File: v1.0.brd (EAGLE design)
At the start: 160 x 100 mm, 142 parts, among them J1 DC-044-A, J2 MICROSD-9P, J3 2p-2.54, J4 2p-2.54, Q1 SI4532ADY, Q3 6pF@32.7680kHz, U1 MCP23017-E/SO, U10 74HC139N, U11 BZX84C30, U2 MCP79412-I/SN, U3 LOPY, U4 GROVE_DC&DC, U5 LM1085IT-5.0, U6 FT232RL-SSOP28, U7 2x14p-2.54, U8 FT232RL-SSOP28, U9 SP483ECN-L, X1 JST-XH-05-PIN-ROUND-PAD, X10 JST-XH-07-PIN-ROUND-PAD, X11 JST-XH-07-PIN-ROUND-PAD, X12 JST-XH-07-PIN-ROUND-PAD, X13 JST-XH-05-PIN-ROUND-PAD, X14 JST-XH-05-PIN-ROUND-PAD, X15 JST-XH-05-PIN-ROUND-PAD, X16 JST-XH-05-PIN-ROUND-PAD, X17 JST-XH-05-PIN-ROUND-PAD, X18 JST-XH-05-PIN-ROUND-PAD, X19 JST-XH-05-PIN-ROUND-PAD, X2 JST-XH-05-PIN-ROUND-PAD, X20 JST-XH-05-PIN-ROUND-PAD, X21 JST-XH-05-PIN-ROUND-PAD, X23 JST-XH-05-PIN-ROUND-PAD, X24 JST-XH-07-PIN-ROUND-PAD, X25 JST-XH-07-PIN-ROUND-PAD, X26 JST-XH-07-PIN-ROUND-PAD, X27 JST-XH-07-PIN-ROUND-PAD, X28 JST-XH-05-PIN-ROUND-PAD, X3 JST-XH-05-PIN-ROUND-PAD, X4 JST-XH-07-PIN-ROUND-PAD, X5 JST-XH-07-PIN-ROUND-PAD, X6 JST-XH-07-PIN-ROUND-PAD, X7 JST-XH-07-PIN-ROUND-PAD, X8 JST-XH-07-PIN-ROUND-PAD, X9 JST-XH-07-PIN-ROUND-PAD

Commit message: polyfuses
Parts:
- removed X26: JST-XH-07-PIN-ROUND-PAD, Rembrandt Electronics - JST XH Connectors v1-0 2:JST-XH-07-PACKAGE-ROUND-PAD
- added F23, F24, F25, F26, F27, F28, F29, F30, F31, F32, F33, F34, F35, F36, F37, F38, F39, F40, F41, F42, F43, F44, F45, F46, F47: SMD1206R500SF, Seeed-Fuse:F1206
- added X22: JST-XH-07-PIN-ROUND-PAD, Rembrandt Electronics - JST XH Connectors v1-0 2:JST-XH-07-PACKAGE-ROUND-PAD
- moved X12 1177.6 mm to (-1008.4, -552.5)
- moved X10 1103.3 mm to (-1008.4, -529.6)
- moved X25 984.9 mm to (-1033.8, -621.0)
- moved X24 981.9 mm to (-1033.8, -598.2)
- moved F2 268.6 mm to (-1022.4, -518.2)
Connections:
- new net +5V1: F24.1, F24.2, X10.1
- new net +5V2: F30.1, F30.2, X12.1
- new net +5V3: F40.1, F40.2, X22.1
- new net +5V4: F42.1, F42.2, X24.1
- new net +5V5: F44.1, F44.2, X25.1
- new net 3V3_SMOOTH1: F27.1, F27.2, X10.2
- new net 3V3_SMOOTH2: F31.1, F31.2, X12.2
- new net 3V3_SMOOTH3: F41.1, F41.2, X22.2
- new net 3V3_SMOOTH4: F43.1, F43.2, X24.2
- new net 3V3_SMOOTH5: F45.1, F45.2, X25.2
- new net N$57: F25.2, X6.2
- new net N$58: F23.2, X6.1
- new net N$59: F3.2, X5.1
- new net N$60: F26.2, X8.1
- new net N$61: F35.2, X23.2
- new net N$62: F47.2, X28.2
- net +5V: now also F23.1, F26.1, F28.1, F28.2, F32.1, F32.2, F34.1, F34.2, F36.1, F36.2, F38.1, F38.2, F46.1, F46.2; no longer X10.1, X12.1, X24.1, X25.1, X26.1, X6.1, X8.1
- net 3V3_SMOOTH: now also F2.1, F2.2, F25.1, F29.1, F29.2, F33.1, F33.2, F35.1, F37.1, F37.2, F39.1, F39.2, F47.1; no longer X10.2, X12.2, X23.2, X24.2, X25.2, X26.2, X28.2, X6.2
- net ADC3+: now also X22.4; no longer X24.4
- net ADC3-: now also X22.5; no longer X24.5
- net ADC4+: now also X22.6; no longer X24.6
- net ADC4-: now also X22.7; no longer X24.7
- net ADC5+: now also X24.4; no longer X25.4
- net ADC5-: now also X24.5; no longer X25.5
- net ADC6+: now also X24.6; no longer X25.6
- net ADC6-: now also X24.7; no longer X25.7
- net ADC7+: now also X25.4; no longer X26.4
- net ADC7-: now also X25.5; no longer X26.5
- net ADC8+: now also X25.6; no longer X26.6
- net ADC8-: now also X25.7; no longer X26.7
- net GND: now also X22.3; no longer X26.3
- net SPI_MISO: now also X10.5, X12.5; no longer X10.4, X12.4
- net SPI_MOSI: now also X10.4, X12.4; no longer X10.5, X12.5

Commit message: I think I am done?
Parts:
- added SW1, SW2: SW-200D, Seeed-Switch:SW2-12.7-12.0X3.6X3.6MM
- R10, R9: value 1K -> 100R; device Seeed-Resistor-2016:R0603 -> Seeed-Resistor:PR-D2.3XL6.5MM
- R6: value 1K -> 220R; device Seeed-Resistor-2016:R0603 -> Seeed-Resistor:PR-D2.3XL6.5MM
- R7: value 1K -> 330K; device Seeed-Resistor-2016:R0603 -> Seeed-Resistor:PR-D2.3XL6.5MM
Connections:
- new net N$65: Q1.1, R17.1, SW2.1
- net GND: now also SW1.2, SW2.2; no longer Q1.1, R17.1
- net N$23: now also SW1.1

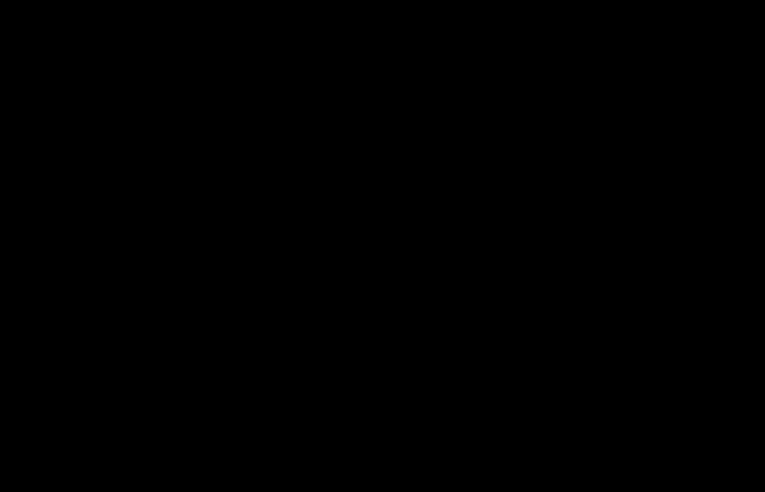
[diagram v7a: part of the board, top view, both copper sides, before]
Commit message: overvoltage
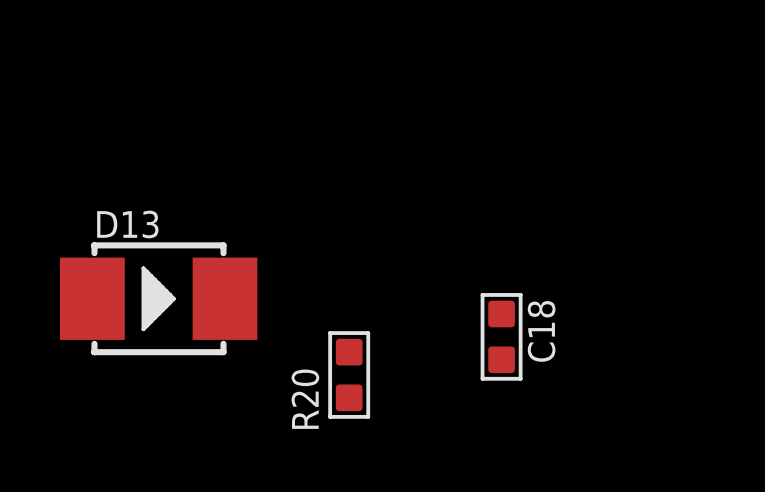
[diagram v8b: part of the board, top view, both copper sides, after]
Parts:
- added C18: 100nf, Seeed-Capacitor:C0603
- added D13: 28V-5A, Seeed-Diode-2016:DO-214AA
- added R20: 15K 1/10W, Seeed-Resistor:R0603
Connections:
- net +24V: now also D13.+
- net GND: now also C18.1, C18.2, D13.-, R20.1, R20.2
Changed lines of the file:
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@@
 <attribute name="MPN" value="SW-200D" x="-1049.02" y="-656.59" size="1.778" layer="27" display="off"/>
+</element>
+<element name="C18" library="Seeed-Capacitor" library_urn="urn:adsk.eagle:library:464" package="C0603" value="100nf" x="-1065.53" y="-659.13">
+<attribute name="MPN" value="CC0603KRX7R9BB104" x="-1065.53" y="-659.13" size="1.778" layer="27" display="off"/>
+</element>
+<element name="R20" library="Seeed-Resistor" library_urn="urn:adsk.eagle:library:474" package="R0603" value="15K 1/10W" x="-1070.61" y="-660.4">
+<attribute name="MPN" value="RC0603FR-0715KL" x="-1070.61" y="-660.4" size="1.778" layer="27" display="off"/>
+</element>
+<element name="D13" library="Seeed-Diode-2016" library_urn="urn:adsk.eagle:library:453" package="DO-214AA" value="28V-5A" x="-1076.96" y="-657.86">
+<attribute name="MPN" value="SS54B" x="-1076.96" y="-657.86" size="1.778" layer="27" display="off"/>
 </element>
 </elements>
@@
 <contactref element="X27" pad="3"/>
 <contactref element="X28" pad="3"/>
-<contactref element="U11" pad="3"/>
 <contactref element="X14" pad="3"/>
 <contactref element="X15" pad="3"/>
@@
 <contactref element="SW1" pad="2"/>
 <contactref element="SW2" pad="2"/>
+<contactref element="U11" pad="3"/>
+<contactref element="R20" pad="2"/>
+<contactref element="D13" pad="-"/>
+<contactref element="C18" pad="2"/>
+<contactref element="R20" pad="1"/>
+<contactref element="C18" pad="1"/>
 <wire x1="-909.32" y1="-325.12" x2="-909.32" y2="-354.33" width="0" layer="19" extent="1-1"/>
 <wire x1="-909.32" y1="-295.91" x2="-909.32" y2="-325.12" width="0" layer="19" extent="1-1"/>
@@
 <wire x1="-1055.37" y1="-642.62" x2="-1036.32" y2="-621.03" width="0" layer="19" extent="1-1"/>
 <wire x1="-1055.37" y1="-656.59" x2="-1055.37" y2="-642.62" width="0" layer="19" extent="1-1"/>
+<wire x1="-1065.53" y1="-658.368" x2="-1055.37" y2="-656.59" width="0" layer="19" extent="1-1"/>
+<wire x1="-1065.53" y1="-659.892" x2="-1065.53" y2="-658.368" width="0" layer="19" extent="1-1"/>
+<wire x1="-1070.61" y1="-659.638" x2="-1065.53" y2="-659.892" width="0" layer="19" extent="1-1"/>
+<wire x1="-1070.61" y1="-661.162" x2="-1070.61" y2="-659.638" width="0" layer="19" extent="1-1"/>
+<wire x1="-1074.75" y1="-657.86" x2="-1070.61" y2="-659.638" width="0" layer="19" extent="1-1"/>
 <wire x1="-142.494" y1="-269.24" x2="-909.32" y2="-295.91" width="0" layer="19" extent="1-1"/>
 <wire x1="-134.62" y1="-255.27" x2="-142.494" y2="-269.24" width="0" layer="19" extent="1-1"/>
@@
 <contactref element="R5" pad="2"/>
 <contactref element="U11" pad="1"/>
+<contactref element="D13" pad="+"/>
+<wire x1="-144.526" y1="-268.3256" x2="-1079.17" y2="-657.86" width="0" layer="19" extent="1-1"/>
 <wire x1="-73.66" y1="72.39" x2="-144.526" y2="-268.3256" width="0" layer="19" extent="1-1"/>
 <wire x1="-73.66" y1="74.93" x2="-73.66" y2="72.39" width="0" layer="19" extent="1-1"/>
